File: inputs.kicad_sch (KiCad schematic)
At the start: 16 parts, among them J1 GFX_Connector_Input, U17 MC34063, U2 74HCT04, U7 74HC32

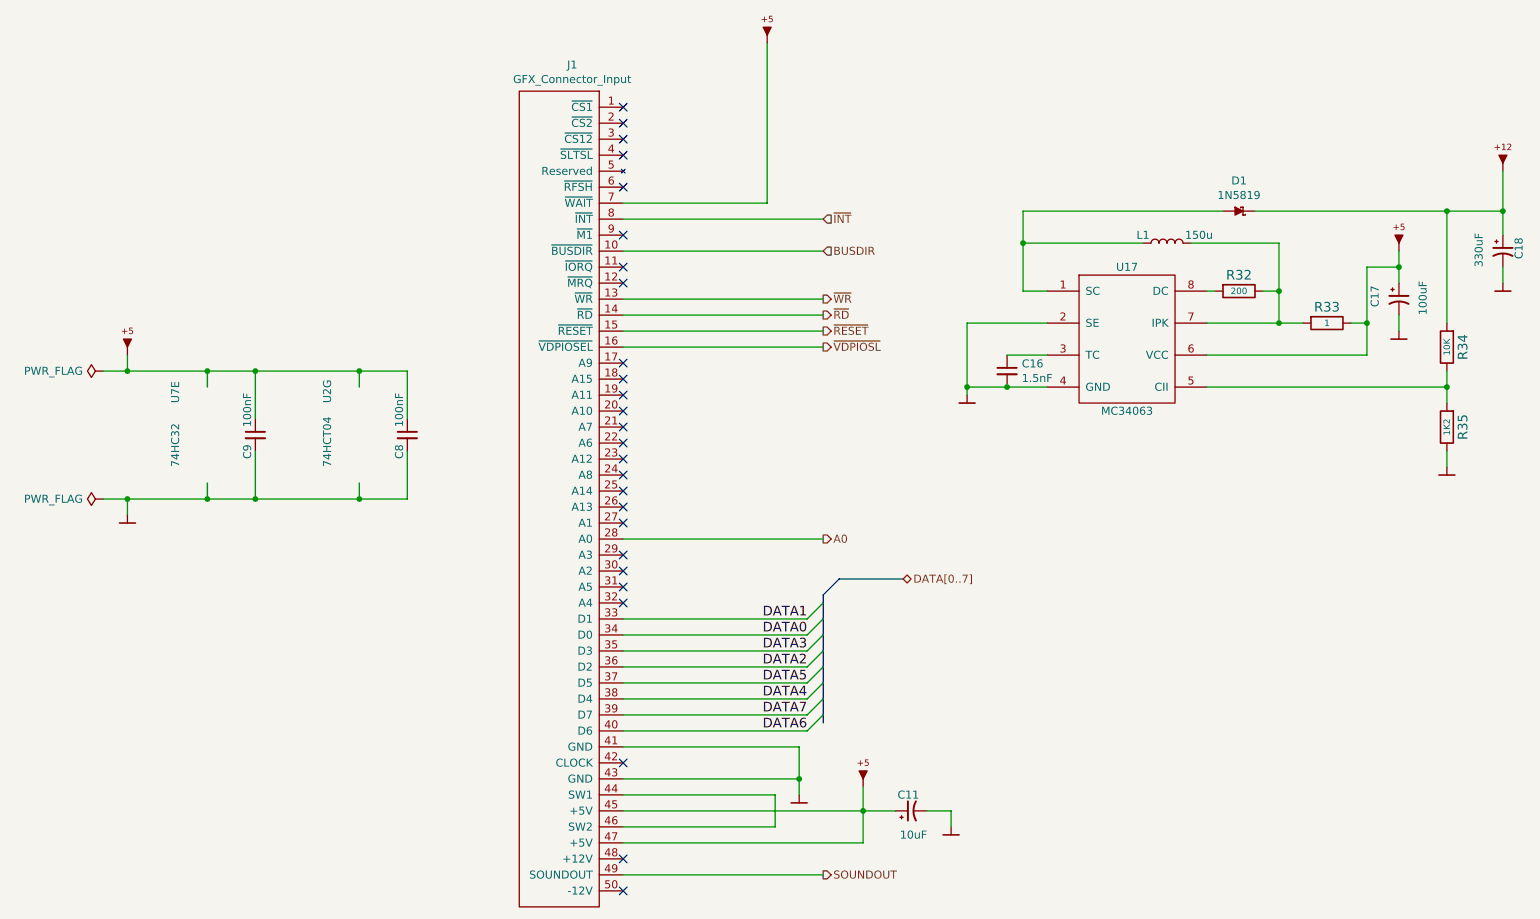
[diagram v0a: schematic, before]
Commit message: Update to latest Artemisa kicadlibs
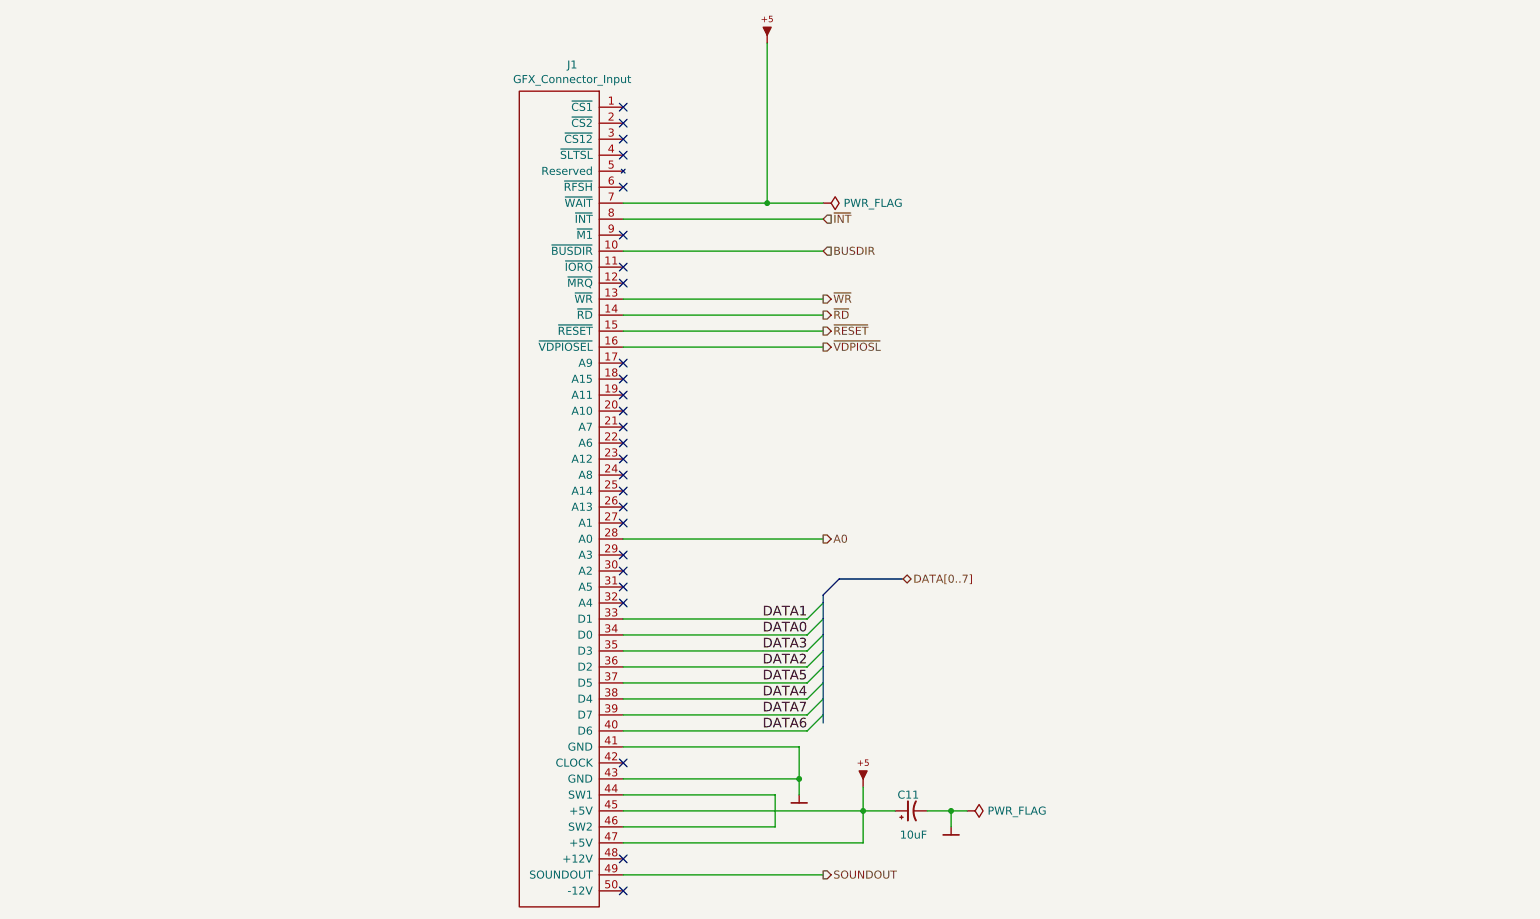
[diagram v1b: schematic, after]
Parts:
- removed C16: 1.5nF, symbol artemisa:Cap
- removed C17: 100uF, artemisa:Radial_capacitor, symbol artemisa:CP
- removed C18: 330uF, artemisa:Radial_capacitor, symbol artemisa:CP
- removed C8, C9: 100nF, artemisa:Disc_capacitor, symbol artemisa:Cap
- removed D1: 1N5819, symbol artemisa:1N5819
- removed L1: 150u, symbol artemisa:L
- removed R32: 200, symbol artemisa:R
- removed R33: 1, symbol artemisa:R
- removed R34: 10K, symbol artemisa:R
- removed R35: 1K2, symbol artemisa:R
- removed U17: MC34063, symbol artemisa:MC34063
- removed U2: 74HCT04, artemisa:DIP-14_300, symbol artemisa:74HCT04
- removed U7: 74HC32, artemisa:DIP-14_300, symbol artemisa:74HC32

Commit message: Use spare MCP6294 as CSYNC buffer
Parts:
- C11: footprint artemisa:Radial_capacitor -> PCM_artemisa:Radial_capacitor
- J1: footprint artemisa:GFX_conn -> PCM_artemisa:GFX_conn; symbol artemisa:GFX_Connector_Input -> PCM_artemisa:GFX_Connector_Input
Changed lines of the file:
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@@
 	)
 	(symbol
-		(lib_id "artemisa:GFX_Connector_Input")
+		(lib_id "PCM_artemisa:GFX_Connector_Input")
 		(at 125.73 102.87 0)
 		(unit 1)
@@
 			)
 		)
-		(property "Footprint" "artemisa:GFX_conn"
+		(property "Footprint" "PCM_artemisa:GFX_conn"
 			(at 119.38 72.39 0)
 			(hide yes)
@@
 			)
 		)
-		(property "Footprint" "artemisa:Radial_capacitor"
+		(property "Footprint" "PCM_artemisa:Radial_capacitor"
 			(at 181.61 148.59 0)
 			(hide yes)
